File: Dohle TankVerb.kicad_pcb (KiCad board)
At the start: 2 copper layers, 53 x 102.4 mm, 10 parts, among them J1 AudioJack3, J2 AudioJack3, J3 PWR, J4 Conn_01x07_Female, SW1 3pdt_footswitch, SW2 SW_Push

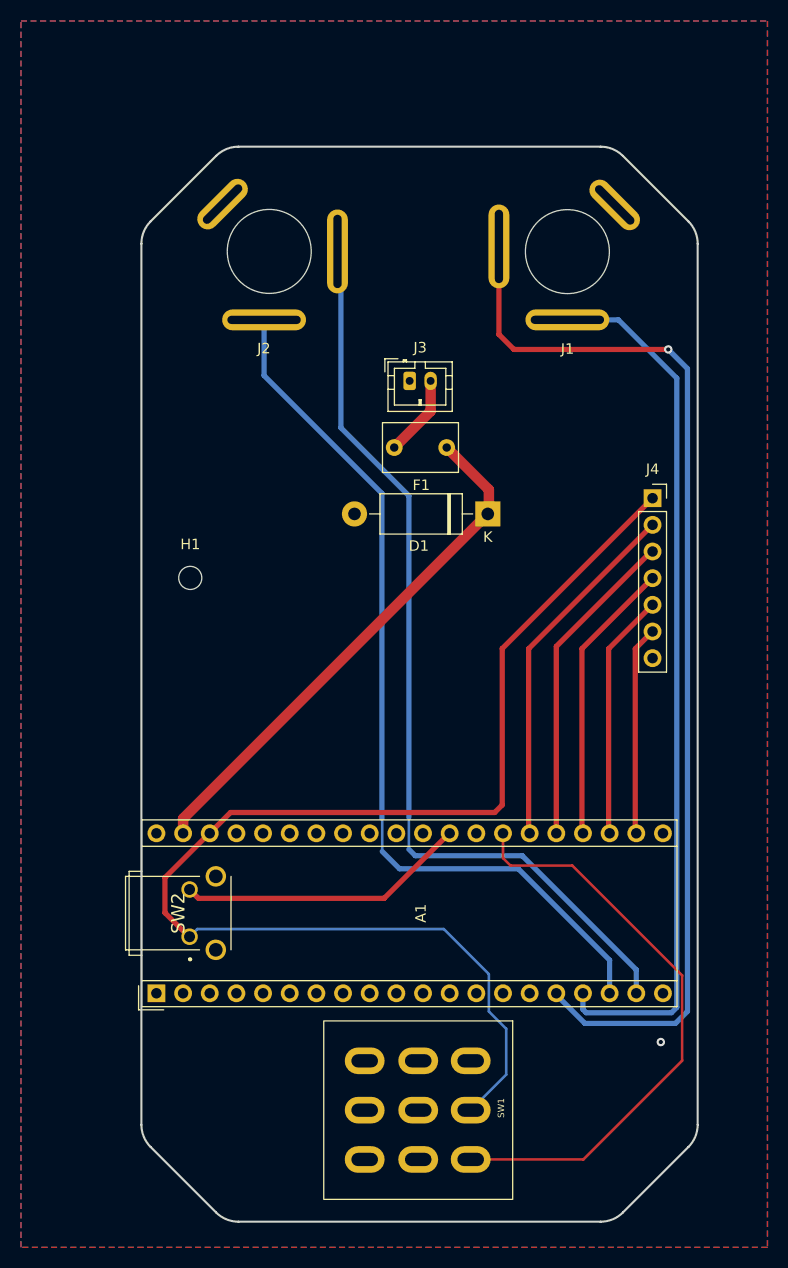
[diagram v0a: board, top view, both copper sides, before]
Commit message: Move components to make space for the pedal plug
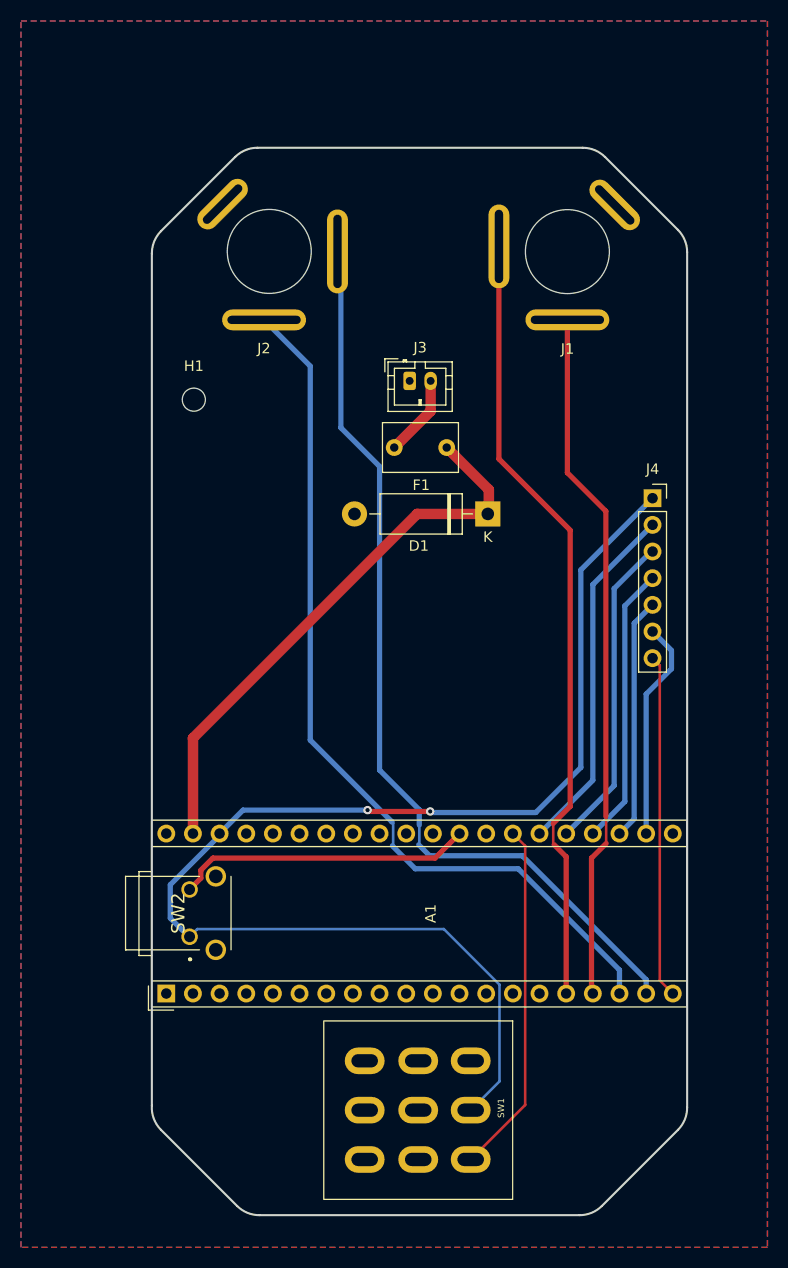
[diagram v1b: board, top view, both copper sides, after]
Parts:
- moved H1 17.0 mm to (135.8, 76.7)
- moved A1 0.94 mm to (133.2, 133.3)
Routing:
- net GND: track 0.00 -> 32.8 mm, vias 1 -> 0
- net FXInL: track 103.2 -> 75.2 mm, vias 1 -> 0
- net SW: track 56.2 -> 33.7 mm
- net FXInR: track 83.5 -> 66.3 mm
- net +9V: track 50.5 -> 54.1 mm
- net POT1: track 19.9 -> 21.0 mm
- net +3V3: track 122.5 -> 123.4 mm, vias 0 -> 2
- net BOOT: track 27.7 -> 28.4 mm
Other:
- board size 53 x 102.4 mm -> 51 x 101.7 mm
- board text added: "v1.1"
- board text removed: "v1.0b"

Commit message: Finish adding the expression pedal. New release.
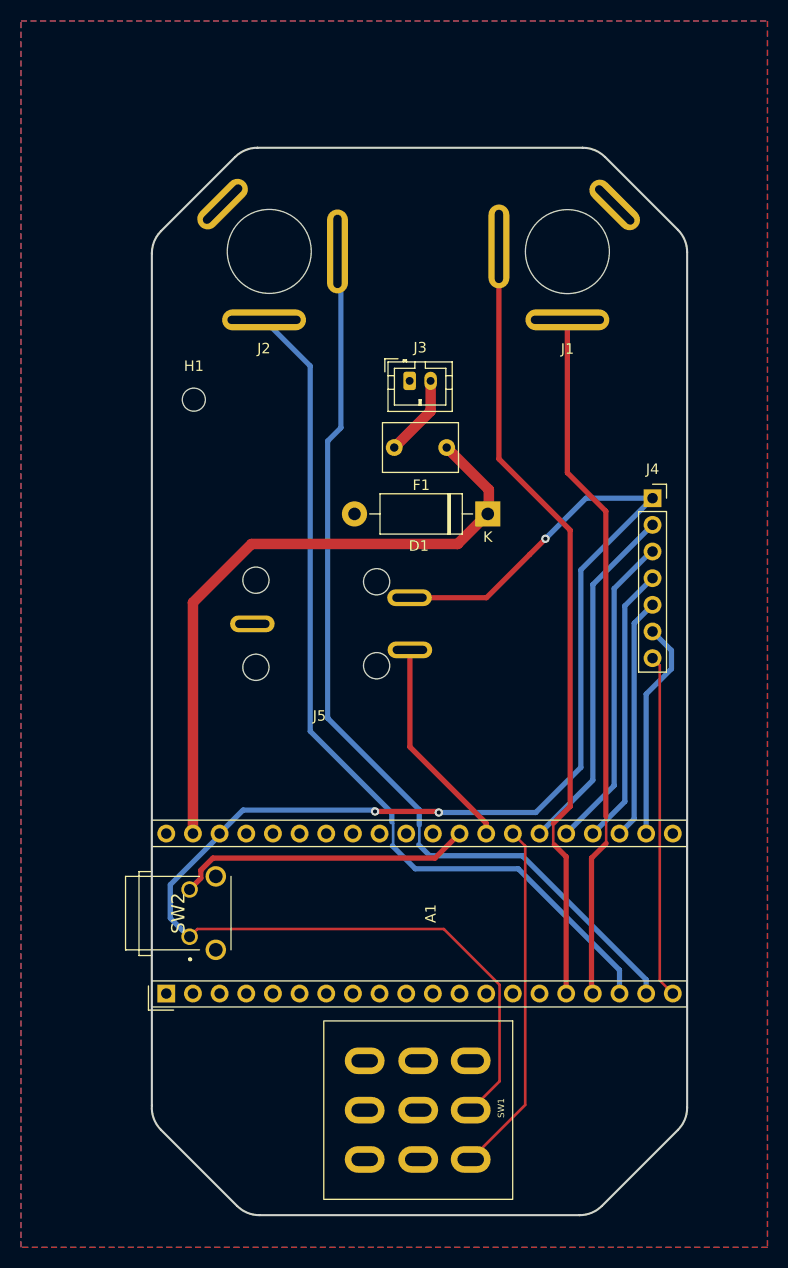
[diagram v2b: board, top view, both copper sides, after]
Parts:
- added J5: ExpressionJack, BirdFootprints:ExpressionJack, F.Cu at (147.8, 107.3)
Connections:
- A1 pad 28: unconnected-(A1-Pad28) -> EXPRESSION
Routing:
- net +3V3: track 123.4 -> 150.5 mm, vias 2 -> 3
- net EXPRESSION: track 0.00 -> 20.5 mm
- net +9V: track 54.1 -> 61.6 mm
- net FXOutR: track 88.1 -> 89.1 mm
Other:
- board text added: "Made in Switzerland"
